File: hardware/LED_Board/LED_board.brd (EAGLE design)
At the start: 50 x 63 mm, 116 parts, among them U1 IS31FL3731-SALS2, U5 MSL0402RGBU1

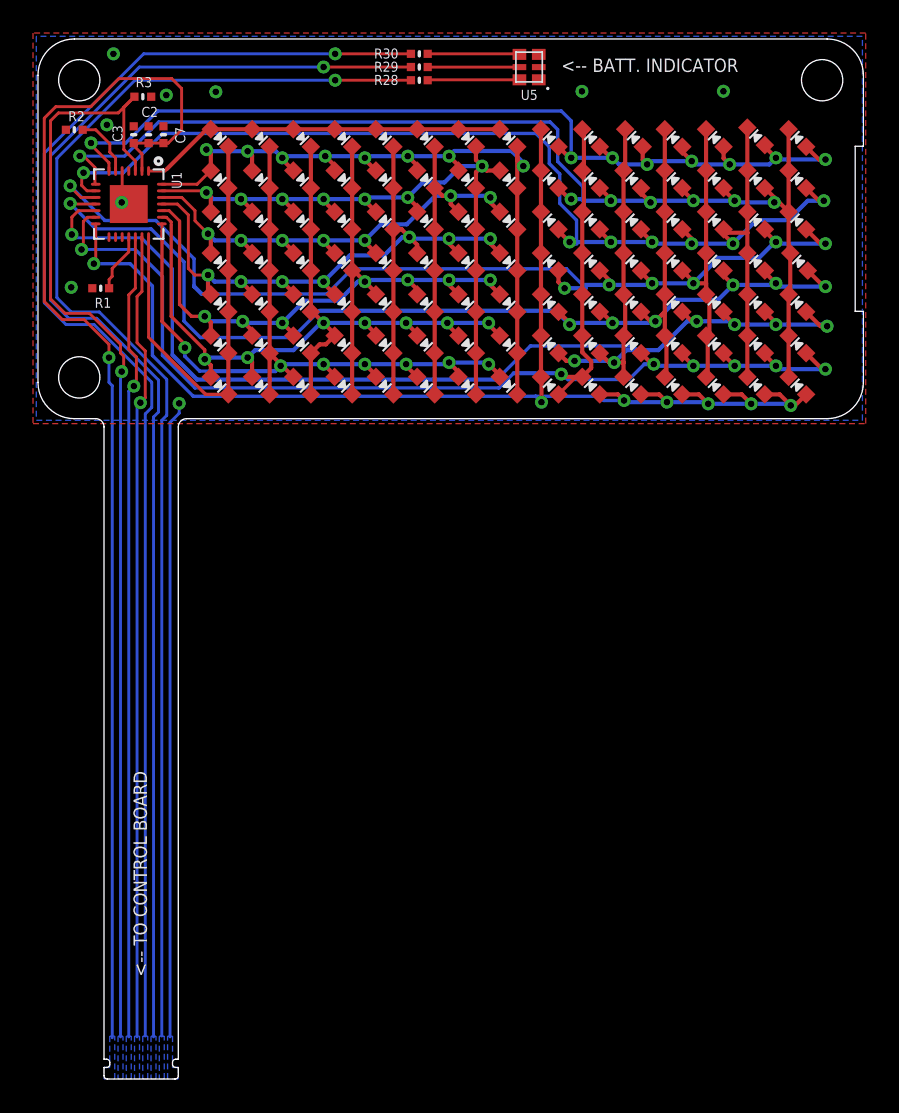
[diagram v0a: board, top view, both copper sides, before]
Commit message: Merged control board and power board, updated LED board
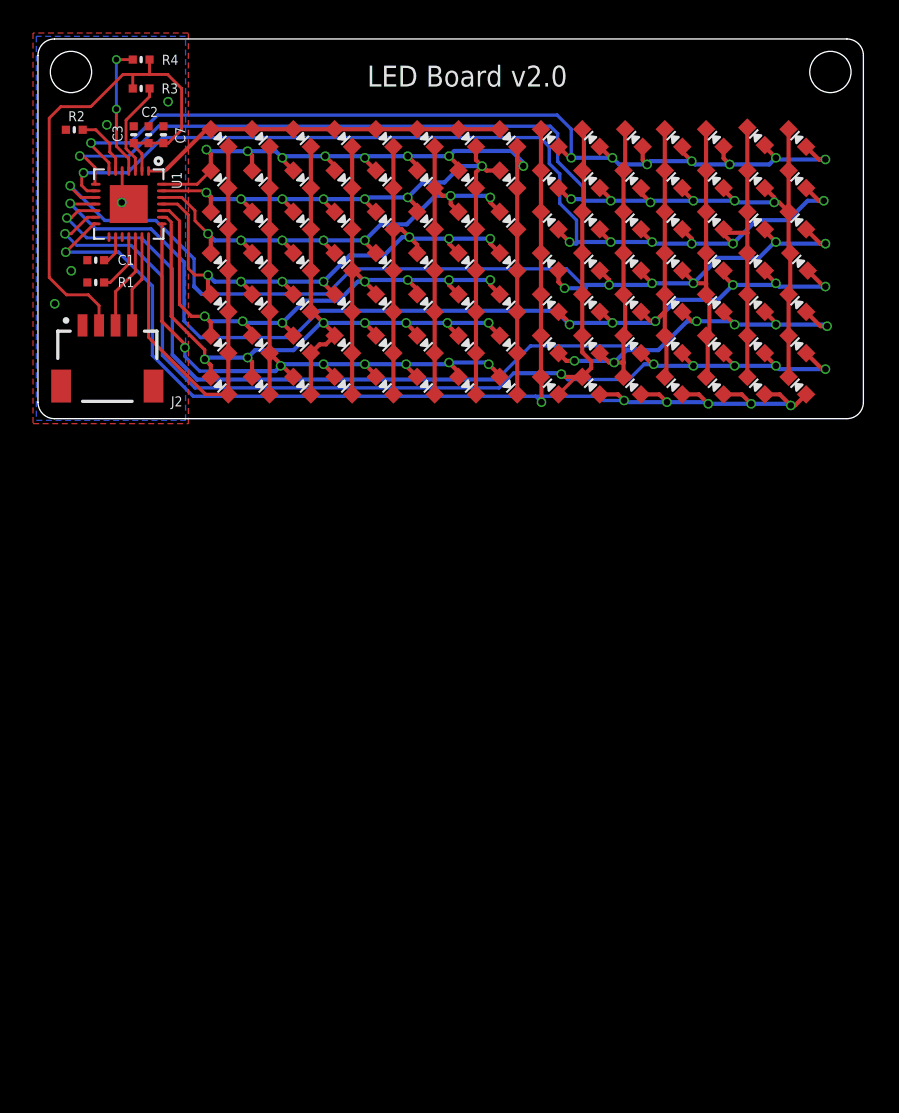
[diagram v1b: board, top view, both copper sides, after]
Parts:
- removed R28, R29, R30: 1K, Adafruit Feather 32u4 Bluefruit LE:MICROBUILDER__0402MP
- removed U5: MSL0402RGBU1, MSL0402RGBU1:SMD-6
- added C1: 0.1uF, Adafruit Feather 32u4 Bluefruit LE:MICROBUILDER__0402MP
- added J2: QWIIC_RIGHT_ANGLE, SparkFun-Connectors:JST04_1MM_RA
- added R4: 10K, Adafruit Feather 32u4 Bluefruit LE:MICROBUILDER__0402MP
- moved R3 0.51 mm to (6.25, 20.0)
- moved R1 0.46 mm to (3.50, 8.25)
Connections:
- removed net BLUE: R28.2
- removed net GREEN: R29.2
- removed net N$16: R28.1, U5.B+
- removed net N$18: R30.1, U5.R+
- removed net N$24: R29.1, U5.G+
- removed net RED: R30.2
- removed net SDB: R3.1, U1.3
- removed net VCC: C2.1, C3.1, C7.1, U1.2
- new net DISPLAY_POWER: C2.1, C3.1, C7.1, J2.2, R3.1, R4.2, U1.2
- new net N$1: R3.2, U1.3
- new net N$2: C1.1, U1.16
- new net N$3: R4.1, U1.4
- net GND: now also C1.2, J2.1; no longer R3.2, U5.B-, U5.G-, U5.R-
- net SCL: now also J2.4
- net SDA: now also J2.3
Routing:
- net RED: track 82.0 -> 0.00 mm, vias 1 -> 0
- net GREEN: track 81.3 -> 0.00 mm, vias 1 -> 0
- net BLUE: track 80.5 -> 0.00 mm, vias 1 -> 0
- net VCC: track 75.4 -> 0.00 mm, vias 1 -> 0
- net SDB: track 69.0 -> 0.00 mm, vias 1 -> 0
- net SCL: track 49.0 -> 5.60 mm, vias 1 -> 0
- net SDA: track 49.0 -> 5.85 mm, vias 1 -> 0
- net GND: track 40.5 -> 1.93 mm, vias 9 -> 5
- net DISPLAY_POWER: track 0.00 -> 33.4 mm
- net N$3: track 0.00 -> 8.05 mm, vias 0 -> 2
- net N$1: track 0.00 -> 5.82 mm
- net N$18: track 5.57 -> 0.00 mm
- net N$16: track 5.57 -> 0.00 mm
- net N$24: track 5.56 -> 0.00 mm
- net CB8: track 77.9 -> 80.0 mm
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- removed copper zone on layer 16, net BLUE
- removed copper zone on layer 16, net GREEN
- removed copper zone on layer 16, net RED
- removed copper zone on layer 16, net SCL
- removed copper zone on layer 16, net SDA
- removed copper zone on layer 16, net SDB
- removed copper zone on layer 16, net VCC
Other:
- board size 50 x 63 mm -> 50 x 23 mm
- board text added: "Designed by Akram Ali v2.0 | 2023-12-04"
- board text added: "LED Board v2.0"
- board text removed: "<-- BATT. INDICATOR"
- board text removed: "<-- TO CONTROL BOARD"
- board text removed: "Designed by Akram v1.1 | 2020-10-28"
